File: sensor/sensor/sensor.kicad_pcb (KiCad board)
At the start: 4 copper layers, 51.2 x 21 mm, 61 parts, among them J1 RJ12_Shielded, J2 Conn_01x04, J3 Conn_01x06, J4 Conn_01x03_Socket, J5 Conn_01x03_Socket, J6 Conn_01x03_Socket, J7 Conn_01x03_Socket, SW5 SW_Coded_SH-7050, U1 PCA9615DP, U2 LTC4316xDD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

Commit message: added footprints of new sensors and JST/RJ12 connectors into PCB
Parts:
- added C11: 0.1u, Capacitor_SMD:C_0402_1005Metric_Pad0.74x0.62mm_HandSolder, F.Cu at (145.1, 65.7)
- added C12: 4.7u, Capacitor_SMD:C_0603_1608Metric_Pad1.08x0.95mm_HandSolder, F.Cu at (148.9, 64.0)
- added C4: 1u, Capacitor_SMD:C_0603_1608Metric_Pad1.08x0.95mm_HandSolder, F.Cu at (148.9, 61.5)
- added C5: 0.1u, Capacitor_SMD:C_0402_1005Metric_Pad0.74x0.62mm_HandSolder, F.Cu at (145.1, 63.7)
- added IC1: VL53L4CDV0DH_1, VL53L4CD:VL53L4CDV0DH1, F.Cu at (150.5, 57.5)
- added IC2: ISL29125IROZ-T7, ISL29125:ISL29125IROZT7, F.Cu at (153.4, 61.9)
- added J8: RJ12_Shielded, RJ12_Pin_Connector:RJ12_Pin_Connector, F.Cu at (128.0, 57.0)
- added J9: Conn_01x06, Connector_JST:JST_SH_SM06B-SRSS-TB_1x06-1MP_P1.00mm_Horizontal, F.Cu at (126.4, 78.6)
- added R15: 100, Resistor_SMD:R_0402_1005Metric_Pad0.72x0.64mm_HandSolder, F.Cu at (145.1, 55.7)
- added R16: 4.7k, Resistor_SMD:R_0402_1005Metric_Pad0.72x0.64mm_HandSolder, F.Cu at (145.1, 57.7)
- added R20: 10k, Resistor_SMD:R_0402_1005Metric_Pad0.72x0.64mm_HandSolder, F.Cu at (145.1, 59.7)
- added R21: 10k, Resistor_SMD:R_0402_1005Metric_Pad0.72x0.64mm_HandSolder, F.Cu at (145.1, 61.7)

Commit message: pcb
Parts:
- removed the C11 at (82.0, 65.0)
- removed the C12 at (80.3, 64.5)
- removed the C4 at (75.5, 68.6)
- removed the C5 at (71.5, 69.0)
- removed C6: 10u, Capacitor_SMD:C_0603_1608Metric_Pad1.08x0.95mm_HandSolder
- removed D1, D2: LED, LED_SMD:LED_0805_2012Metric_Pad1.15x1.40mm_HandSolder
- removed the R15 at (73.5, 72.6)
- removed the R16 at (77.9, 64.7)
- removed R17, R18: 180, Resistor_SMD:R_0402_1005Metric_Pad0.72x0.64mm_HandSolder
- removed the R20 at (75.0, 72.6)
- removed the R21 at (76.5, 72.6)
- removed U3: APDS-9960, Sensor:Avago_APDS-9960
- removed U7: VL53L1CXV0FY1, Sensor_Distance:ST_VL53L1x
- J9: moved to B.Cu
- moved C4 88.3 mm to (71.5, 104.0), turned to 180 degrees
- moved IC2 88.2 mm to (74.8, 102.0)
- moved R15 87.0 mm to (71.8, 102.7), turned to 180 degrees
- moved J8 85.0 mm to (59.4, 107.3), turned to -90 degrees
- moved C5 82.5 mm to (71.8, 101.7), turned to 180 degrees
- moved IC1 81.8 mm to (82.5, 103.0)
- moved J9 81.3 mm to (51.6, 110.5), turned to -90 degrees
- moved R16 80.8 mm to (77.5, 102.0), turned to 180 degrees
- moved R20 80.5 mm to (77.5, 103.5), turned to 180 degrees
- moved R21 80.1 mm to (77.5, 104.6)
- moved C12 78.0 mm to (83.2, 106.1)
- moved C11 74.6 mm to (83.3, 107.5), turned to 180 degrees
- moved C3 67.3 mm to (63.3, 117.2), turned to 180 degrees
- moved C2 66.1 mm to (65.0, 115.5), turned to 180 degrees
- moved H1 63.9 mm to (94.9, 110.5)
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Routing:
- net GND: track 79.4 -> 0.00 mm, vias 21 -> 0
- net +3.3V: track 73.2 -> 2.97 mm, vias 12 -> 0
- net +5V: track 45.9 -> 6.07 mm, vias 6 -> 0
- net Net-(U2-XORH): track 33.0 -> 4.59 mm, vias 2 -> 0
- net Net-(U2-XORL): track 25.7 -> 4.12 mm, vias 2 -> 0
- net Net-(J3-Pin_5): track 28.2 -> 12.9 mm, vias 2 -> 0
- net Net-(U3-VDD): track 13.2 -> 0.00 mm
- net Net-(J2-Pin_3): track 19.3 -> 30.7 mm, vias 3 -> 1
- net Net-(R12-Pad1): track 18.4 -> 7.42 mm
- net Net-(J3-Pin_3): track 24.0 -> 34.8 mm, vias 2 -> 0
- net Net-(U6-~{CS}): track 11.8 -> 1.24 mm, vias 2 -> 0
- net Net-(J3-Pin_2): track 24.6 -> 14.3 mm
- net Net-(R25-Pad1): track 16.0 -> 6.13 mm
- net Net-(J7-Pin_3): track 9.01 -> 18.3 mm
- net Net-(U5-FB): track 11.9 -> 3.78 mm, vias 2 -> 0
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- removed copper zone on In1.Cu, net +3.3V
- removed copper zone on In1.Cu, net +5V
- removed copper zone on In2.Cu, net GND
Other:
- board size 51.2 x 21 mm -> 71.5 x 21 mm

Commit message: restarting layout
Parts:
- J2: moved to F.Cu
- J8: moved to B.Cu
- moved J9 109.4 mm to (159.5, 92.2), turned to 180 degrees
- moved J8 79.3 mm to (137.1, 91.2)
- moved C2 70.1 mm to (94.1, 51.7), turned to 0 degrees
- moved C3 70.1 mm to (94.1, 54.2), turned to 0 degrees
- moved U5 68.9 mm to (89.3, 52.9)
- moved C4 68.8 mm to (108.8, 46.2), turned to 0 degrees
- moved C8 67.5 mm to (108.8, 48.7)
- moved J3 67.1 mm to (51.1, 92.6), turned to 180 degrees
- moved C10 65.6 mm to (105.1, 51.8), turned to 0 degrees
- moved C7 65.4 mm to (105.1, 47.9)
- moved R10 65.0 mm to (89.5, 57.1), turned to 0 degrees
- moved C5 64.9 mm to (105.1, 45.9), turned to 0 degrees
- moved R15 64.2 mm to (101.8, 45.9), turned to 0 degrees
- moved R8 63.6 mm to (79.5, 53.2)
- moved C9 62.6 mm to (105.1, 49.9)
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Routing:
- net /Sensors/scl: track 46.9 -> 0.00 mm, vias 2 -> 0
- net /Sensors/sda: track 45.9 -> 0.00 mm, vias 2 -> 0
- net Net-(J3-Pin_3): track 34.8 -> 0.00 mm
- net Net-(J2-Pin_3): track 30.7 -> 0.00 mm, vias 1 -> 0
- net Net-(J2-Pin_4): track 29.3 -> 0.00 mm, vias 2 -> 0
- net Net-(J3-Pin_4): track 21.0 -> 0.00 mm
- net Net-(J7-Pin_3): track 18.3 -> 0.00 mm
- net Net-(J3-Pin_2): track 14.3 -> 0.00 mm
- net Net-(J6-Pin_3): track 13.2 -> 0.00 mm
- net Net-(J3-Pin_5): track 12.9 -> 0.00 mm
- net Net-(R24-Pad1): track 10.2 -> 0.00 mm, vias 1 -> 0
- net Net-(J5-Pin_3): track 9.57 -> 0.00 mm
- net Net-(J4-Pin_3): track 8.07 -> 0.00 mm
- net Net-(R13-Pad1): track 7.70 -> 0.00 mm, vias 1 -> 0
- net Net-(R12-Pad1): track 7.42 -> 0.00 mm, vias 1 -> 0
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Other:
- board outline removed

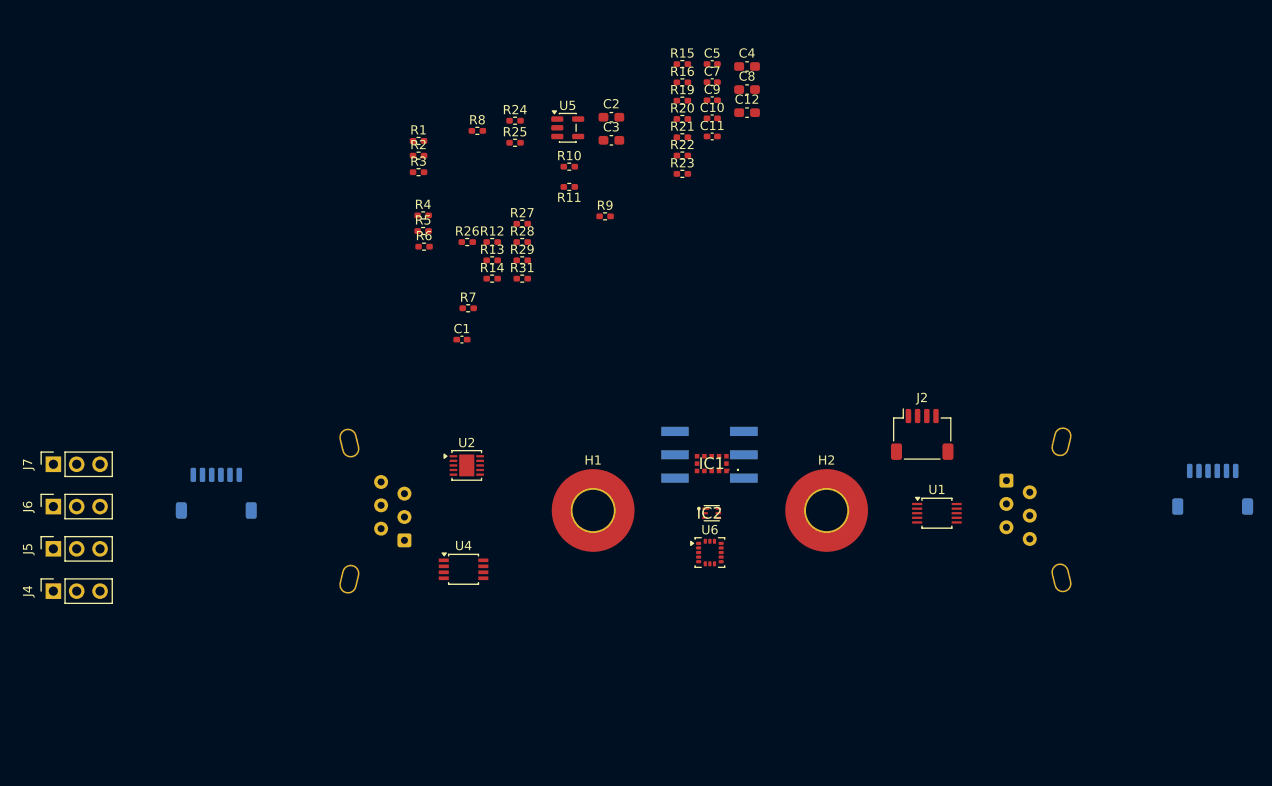
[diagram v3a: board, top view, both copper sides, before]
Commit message: sensor pcb layout, deleted gpio ic
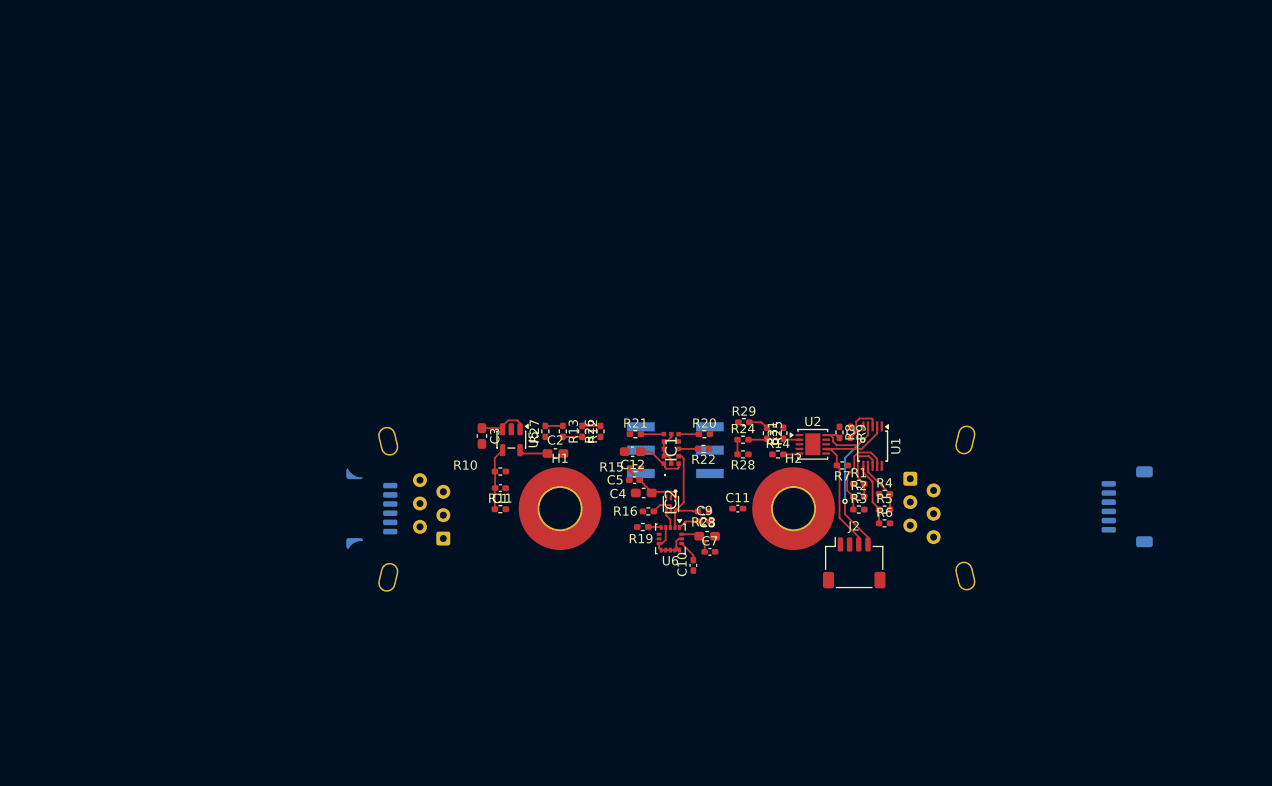
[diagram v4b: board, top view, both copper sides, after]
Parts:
- removed J4, J5, J6, J7: Conn_01x03_Socket, Connector_PinSocket_2.54mm:PinSocket_1x03_P2.54mm_Vertical
- removed U4: PCA9536DP, Package_SO:TSSOP-8_3x3mm_P0.65mm
- moved J3 99.1 mm to (150.2, 94.1), turned to -90 degrees
- moved J9 91.5 mm to (68.0, 94.3), turned to 90 degrees
- moved R1 60.7 mm to (121.0, 91.6)
- moved R2 60.6 mm to (121.0, 93.0)
- moved R3 60.3 mm to (121.0, 94.4)
- moved R4 58.6 mm to (123.8, 92.7)
- moved R5 58.6 mm to (123.8, 94.4)
- moved R6 58.4 mm to (123.8, 95.9)
- moved R8 51.3 mm to (118.9, 86.0), turned to -90 degrees
- moved C7 51.1 mm to (104.8, 99.0)
- moved C8 48.8 mm to (104.5, 97.3)
- moved C10 48.7 mm to (103.0, 100.5), turned to -90 degrees
- moved C4 47.7 mm to (97.6, 92.6), turned to 180 degrees
- moved R16 46.8 mm to (98.1, 94.6)
- moved R19 46.6 mm to (97.5, 96.3)
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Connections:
- R15 pad 2: +3V3 -> +3.3V
- R16 pad 1: +3V3 -> +3.3V
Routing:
- net Net-(J2-Pin_4): track 0.00 -> 21.5 mm, vias 0 -> 2
- net Net-(J2-Pin_3): track 0.00 -> 19.8 mm
- net GND: track 0.00 -> 11.1 mm
- net /Sensors/scl: track 0.00 -> 11.0 mm
- net Net-(J3-Pin_3): track 0.00 -> 10.1 mm
- net +3.3V: track 0.00 -> 9.49 mm
- net Net-(IC2-VDD): track 0.00 -> 7.02 mm
- net Net-(J3-Pin_2): track 0.00 -> 6.99 mm
- net Net-(J3-Pin_5): track 0.00 -> 6.96 mm
- net Net-(U5-FB): track 0.00 -> 6.80 mm
- net Net-(J3-Pin_4): track 0.00 -> 5.74 mm
- net Net-(U2-XORH): track 0.00 -> 5.63 mm
- net +3V3: track 0.00 -> 5.62 mm
- net +5V: track 0.00 -> 5.60 mm
- net Net-(U1-EN): track 0.00 -> 4.74 mm
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
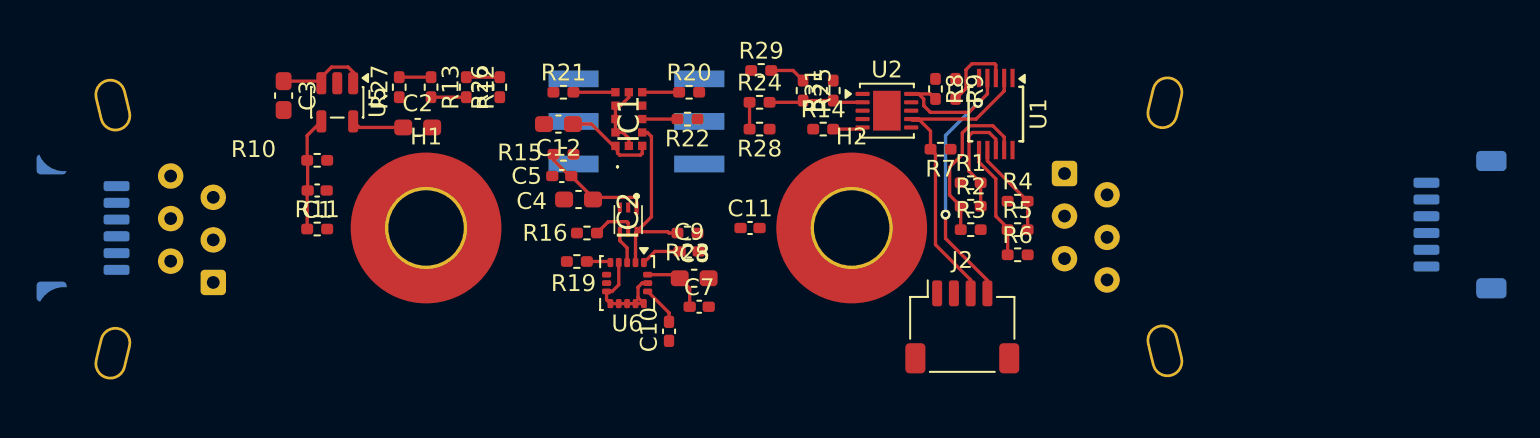
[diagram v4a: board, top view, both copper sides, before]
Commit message: sensor pcb layout
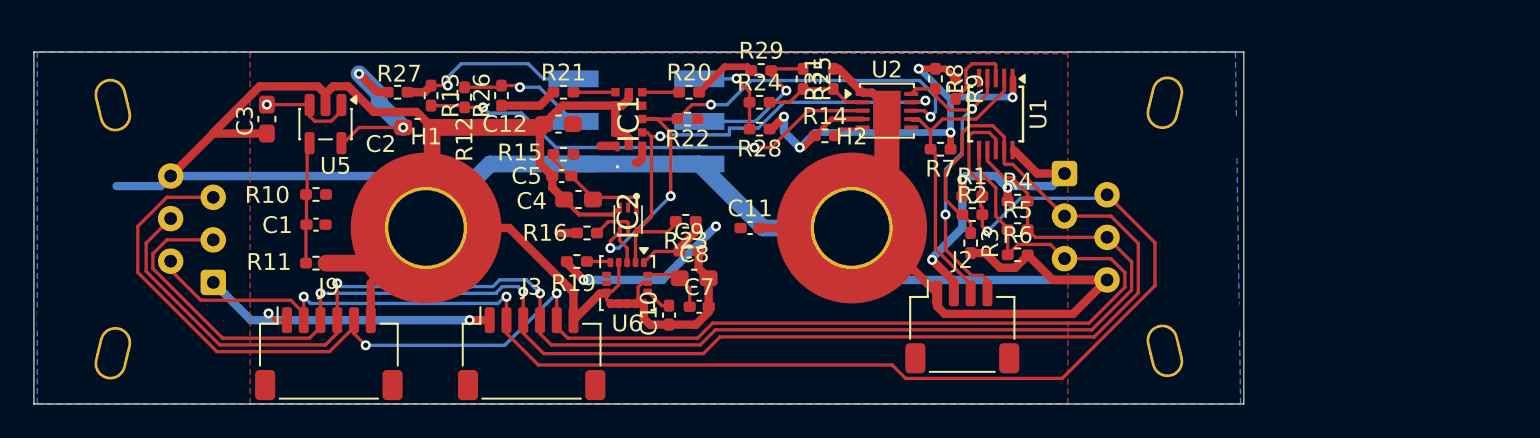
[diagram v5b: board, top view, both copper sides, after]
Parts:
- J3, J9: moved to F.Cu
- moved J3 55.9 mm to (94.8, 101.8), turned to 0 degrees
- moved J9 16.5 mm to (82.7, 101.8), turned to 0 degrees
- moved R11 2.04 mm to (81.9, 96.4)
- moved C1 2.04 mm to (81.9, 94.1)
- moved R10 2.04 mm to (81.9, 92.3)
- moved C3 1.72 mm to (79.0, 87.8)
- moved U5 1.48 mm to (82.5, 88.1)
- moved C10 0.97 mm to (103.0, 99.5)
- moved R1 0.81 mm to (121.1, 92.4)
- moved R3 0.80 mm to (121.0, 95.2), turned to -90 degrees
- moved R23 0.71 mm to (104.0, 93.9)
- moved R25 0.70 mm to (111.0, 85.4)
- moved R31 0.70 mm to (112.8, 85.4)
- moved R12 0.61 mm to (90.8, 86.5)
- moved R8 0.60 mm to (118.9, 85.4)
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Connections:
- C11 pad 1: +3V3 -> +3.3V
- C12 pad 1: +3V3 -> +3.3V
- IC1 pad 1: +3V3 -> +3.3V
- IC1 pad 11: +3V3 -> +3.3V
- IC1 pad 13: +3V3 -> +3.3V
- R20 pad 2: +3V3 -> +3.3V
- R21 pad 1: +3V3 -> +3.3V
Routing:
- net GND: track 11.1 -> 209.4 mm
- net Net-(J3-Pin_3): track 10.1 -> 97.0 mm, vias 0 -> 2
- net Net-(J3-Pin_2): track 6.99 -> 91.6 mm, vias 0 -> 3
- net Net-(J3-Pin_5): track 6.96 -> 91.6 mm, vias 0 -> 2
- net Net-(J3-Pin_4): track 5.74 -> 86.9 mm, vias 0 -> 2
- net +3.3V: track 9.49 -> 70.3 mm, vias 0 -> 9
- net +5V: track 5.60 -> 44.9 mm, vias 0 -> 6
- net /Sensors/sda: track 4.12 -> 35.4 mm, vias 0 -> 4
- net Net-(U2-XORL): track 2.10 -> 27.7 mm, vias 0 -> 2
- net /Sensors/scl: track 11.0 -> 29.6 mm, vias 0 -> 2
- net Net-(R13-Pad1): track 1.90 -> 11.3 mm, vias 0 -> 1
- net Net-(R25-Pad1): track 2.15 -> 9.48 mm, vias 0 -> 1
- net +3V3: track 5.62 -> 0.00 mm
- net Net-(R12-Pad1): track 2.00 -> 7.43 mm, vias 0 -> 1
- net Net-(R24-Pad1): track 1.60 -> 5.57 mm, vias 0 -> 1
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- added copper zone on F.Cu, net +3.3V
- added copper zone on B.Cu, net +5V
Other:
- board outline added: 72.2 x 21 mm

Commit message: sensor pcb layout
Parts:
- added D1: WHITE, LED_SMD:LED_0805_2012Metric_Pad1.15x1.40mm_HandSolder, F.Cu at (108.2, 112.6)
- added D2: WHITE, LED_SMD:LED_0805_2012Metric_Pad1.15x1.40mm_HandSolder, F.Cu at (108.2, 109.5)
- added R17: 120, Resistor_SMD:R_0402_1005Metric, F.Cu at (111.6, 112.6)
- added R18: 120, Resistor_SMD:R_0402_1005Metric, F.Cu at (111.6, 109.6)
- added R30: 120, Resistor_SMD:R_0402_1005Metric, F.Cu at (114.0, 112.6)
- added R32: 120, Resistor_SMD:R_0402_1005Metric, F.Cu at (114.0, 109.6)
- U2: value LTC4316xDD -> LTC4316; footprint Package_DFN_QFN:DFN-10-1EP_3x3mm_P0.5mm_EP1.65x2.38mm -> Package_SO:MSOP-10_3x3mm_P0.5mm
- moved R14 1.62 mm to (110.8, 89.4)
- moved R31 1.60 mm to (111.2, 85.4)
- moved R25 1.10 mm to (109.9, 85.4)
- moved R29 1.02 mm to (107.5, 84.7)
- moved R24 0.91 mm to (107.5, 86.7)
- moved U2 0.91 mm to (115.1, 87.4)
- moved R28 0.70 mm to (107.7, 88.4)
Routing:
- net GND: track 209.4 -> 224.3 mm, vias 0 -> 1
- net /Sensors/sda: track 35.4 -> 31.8 mm
- net +3.3V: track 70.3 -> 73.5 mm
- net /Sensors/scl: track 29.6 -> 27.6 mm
- net Net-(J3-Pin_4): track 86.9 -> 88.8 mm
- net Net-(J3-Pin_3): track 97.0 -> 98.7 mm
- net Net-(J3-Pin_5): track 91.6 -> 92.5 mm
- net Net-(J3-Pin_2): track 91.6 -> 92.4 mm
- net Net-(J2-Pin_4): track 20.0 -> 20.8 mm
- net Net-(R24-Pad1): track 5.57 -> 4.89 mm
- net Net-(U2-XORL): track 27.7 -> 28.2 mm

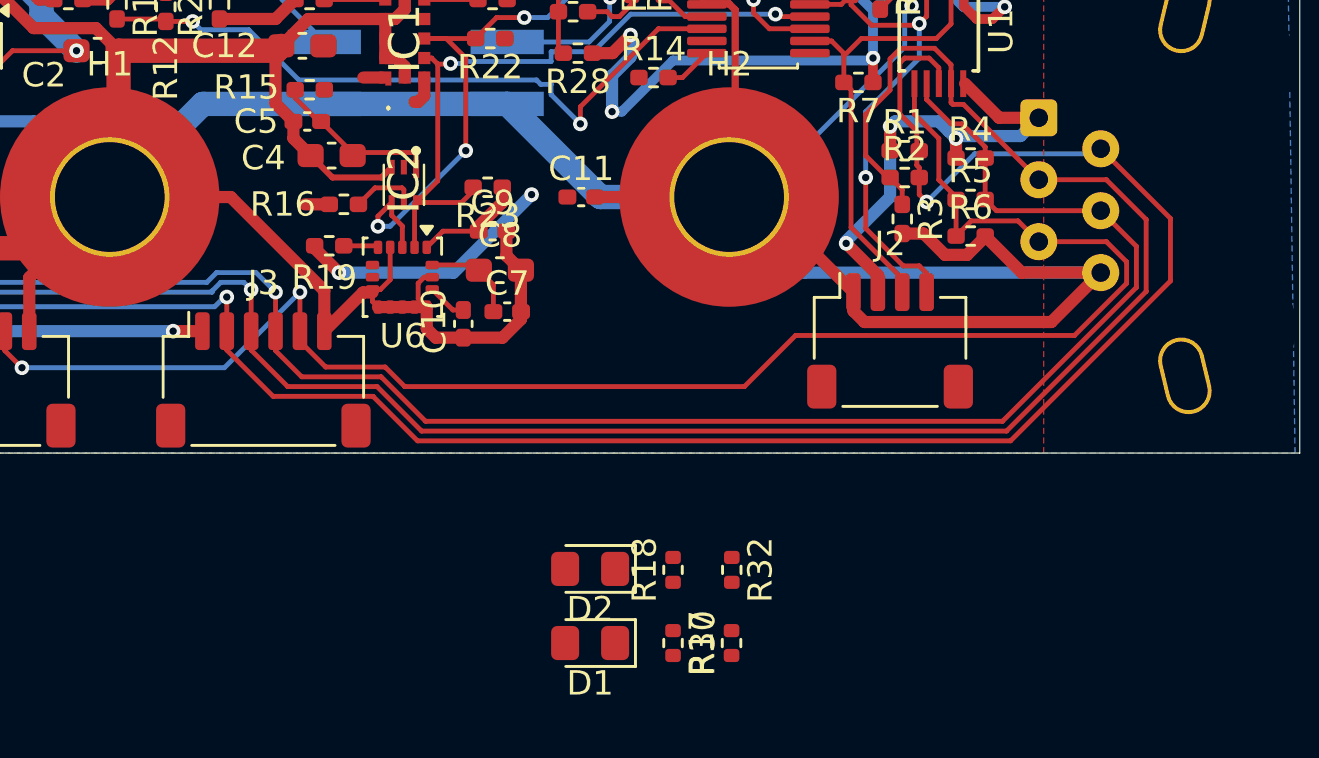
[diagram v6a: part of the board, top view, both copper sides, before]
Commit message: sensor pcb layout
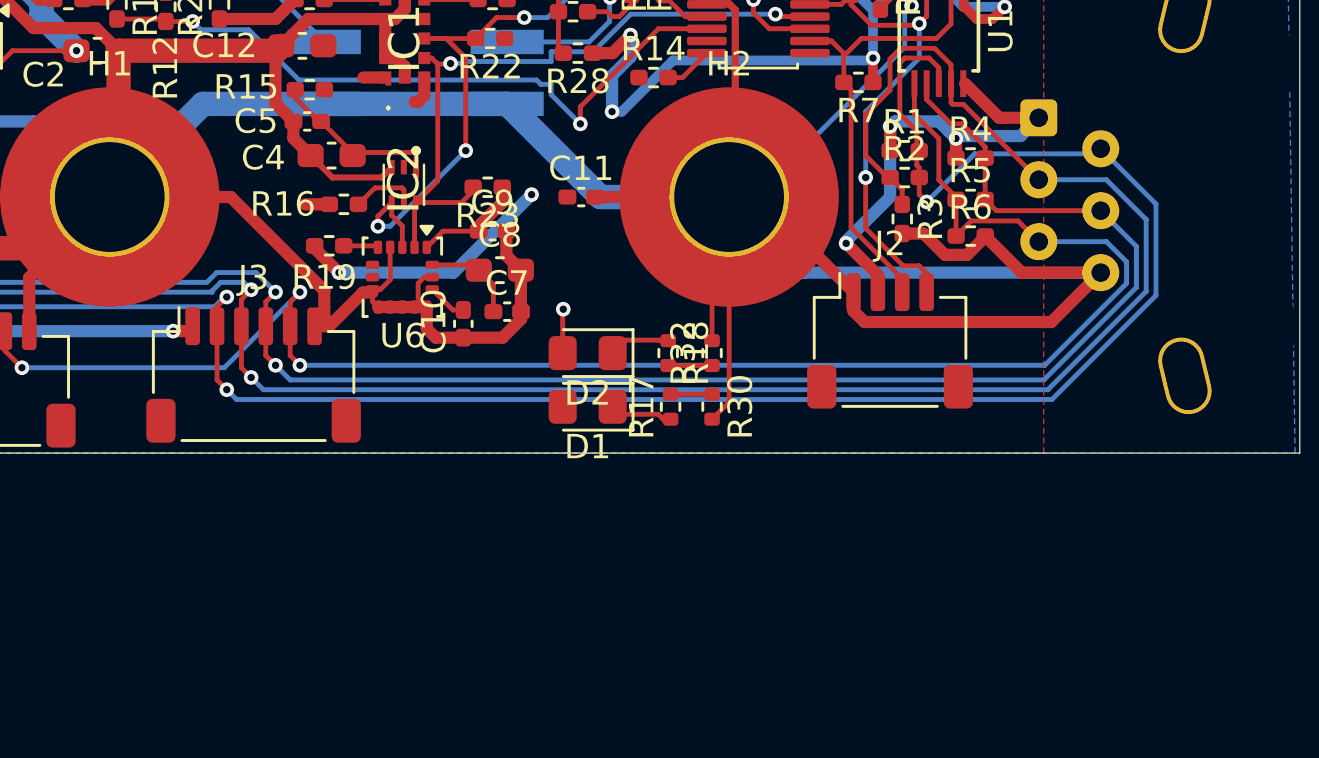
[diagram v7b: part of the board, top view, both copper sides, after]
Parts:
- moved R30 9.72 mm to (113.2, 102.9), turned to -90 degrees
- moved D1 9.69 mm to (108.1, 102.9)
- moved R17 9.69 mm to (111.5, 102.9), turned to 90 degrees
- moved R32 8.93 mm to (113.2, 100.7), turned to 90 degrees
- moved R18 8.89 mm to (111.4, 100.7), turned to -90 degrees
- moved D2 8.85 mm to (108.1, 100.7)
- moved J3 0.45 mm to (94.4, 101.6)
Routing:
- net GND: track 224.3 -> 240.2 mm
- net Net-(D1-K): track 0.00 -> 2.59 mm
- net Net-(D2-K): track 0.00 -> 2.50 mm
- net Net-(R18-Pad2): track 0.00 -> 1.80 mm
- net Net-(R17-Pad2): track 0.00 -> 1.70 mm
- net +5V: track 44.9 -> 46.4 mm, vias 6 -> 7
- net Net-(J3-Pin_4): track 88.8 -> 88.1 mm, vias 2 -> 3
- net Net-(J3-Pin_2): track 92.4 -> 91.8 mm, vias 3 -> 4
- net Net-(J3-Pin_3): track 98.7 -> 98.3 mm, vias 2 -> 3
- net Net-(J3-Pin_5): track 92.5 -> 92.7 mm, vias 2 -> 3
